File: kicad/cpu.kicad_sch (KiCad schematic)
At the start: 10 parts, among them U3 74HC138, U4 W65C02SxP, U6 74HC04, U7 74HC00

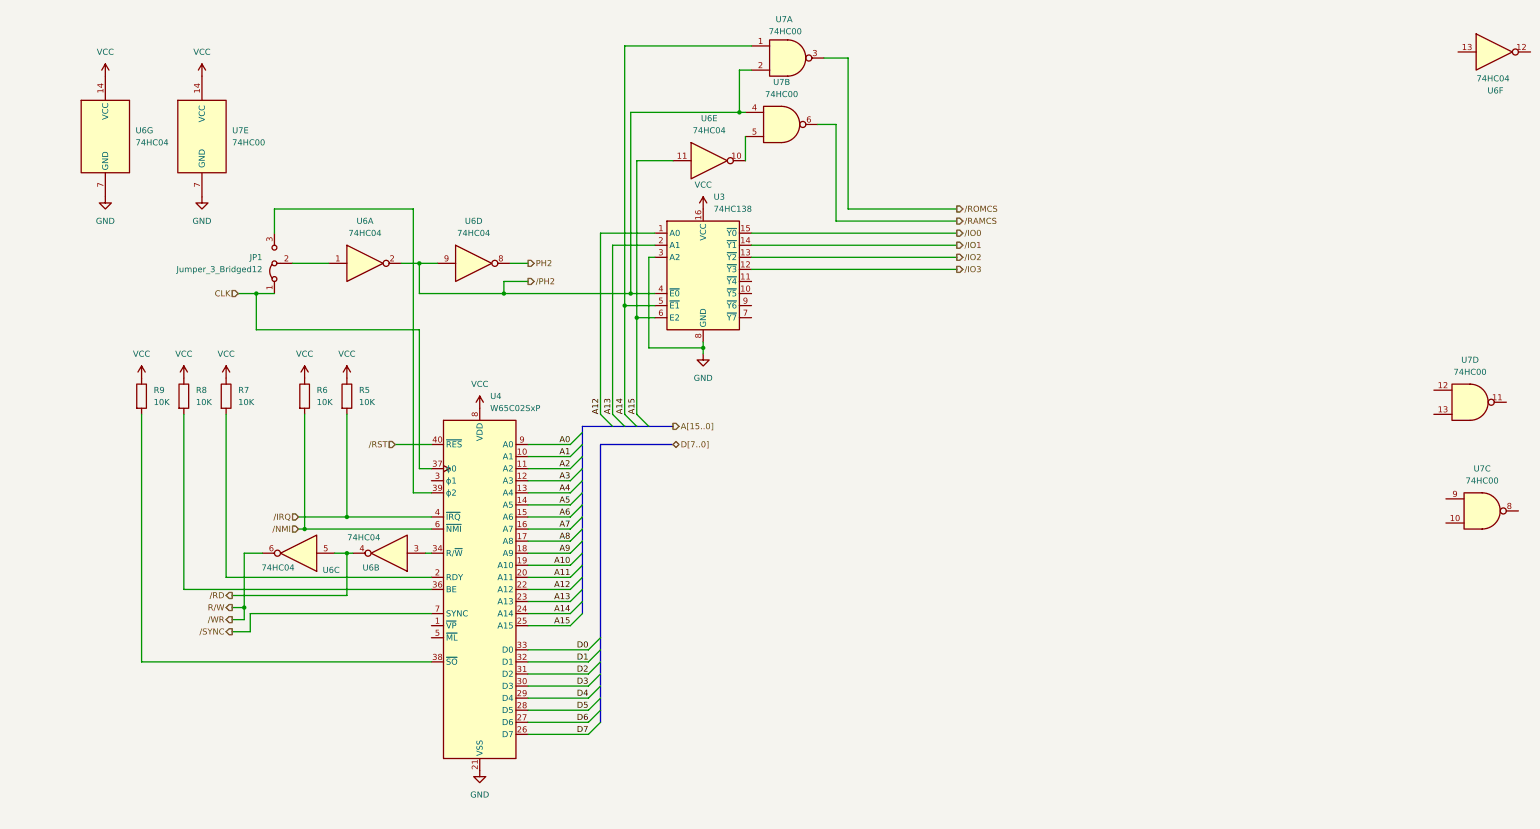
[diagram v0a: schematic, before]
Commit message: Add keyboard connector
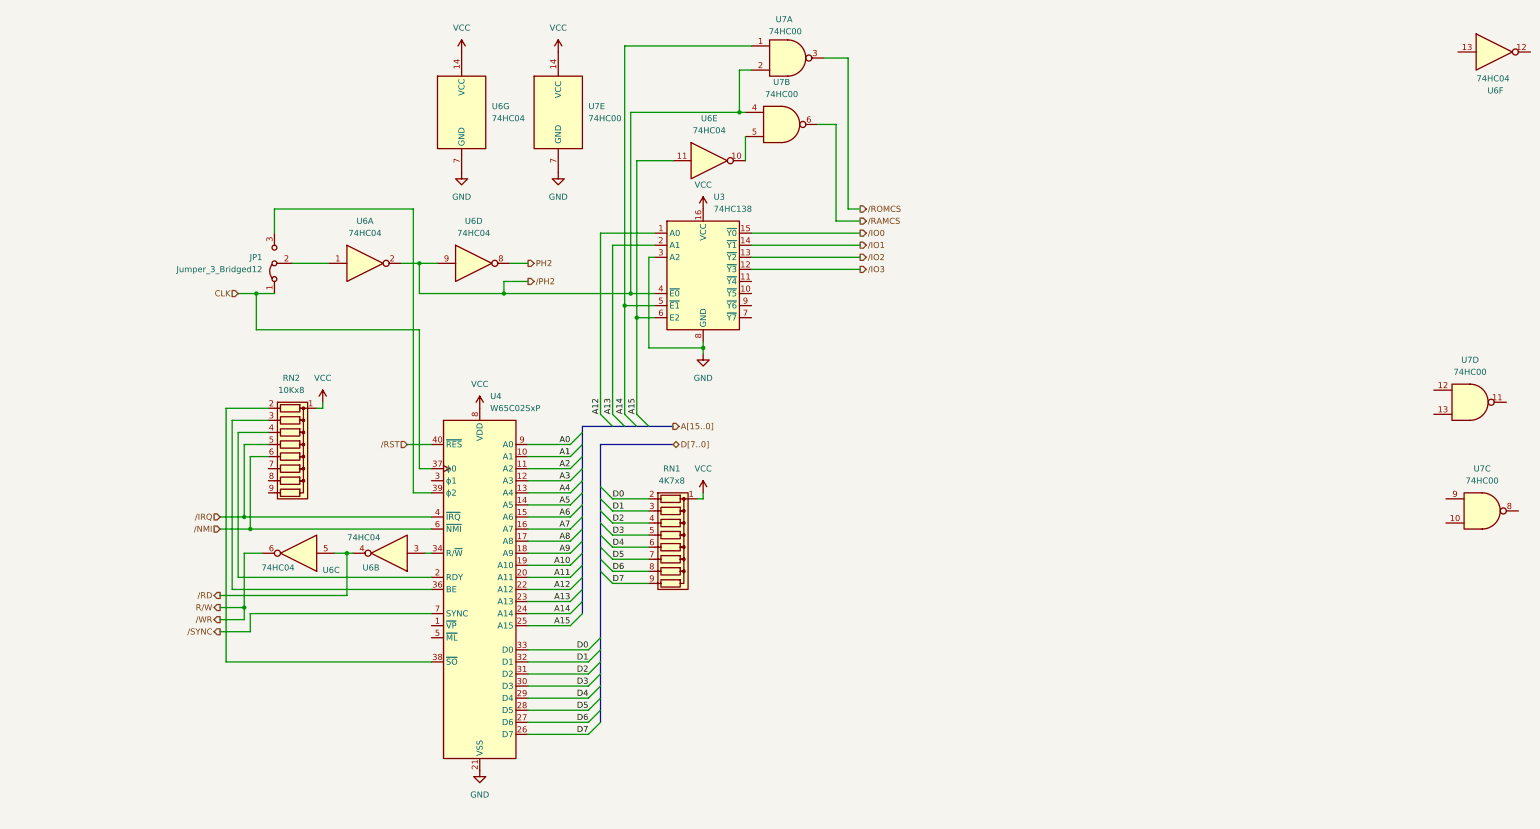
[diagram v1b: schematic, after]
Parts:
- removed R5, R6, R7, R8, R9: 10K, Resistor_THT:R_Axial_DIN0207_L6.3mm_D2.5mm_P7.62mm_Horizontal, symbol Device:R
- added RN1: 4K7x8, Resistor_THT:R_Array_SIP9, symbol Device:R_Network08
- added RN2: 10Kx8, Resistor_THT:R_Array_SIP9, symbol Device:R_Network08
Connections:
- net D0: now also RN1.2 (R1)
- net D1: now also RN1.3 (R2)
- net D2: now also RN1.4 (R3)
- net D3: now also RN1.5 (R4)
- net D4: now also RN1.6 (R5)
- net D5: now also RN1.7 (R6)
- net D6: now also RN1.8 (R7)
- net D7: now also RN1.9 (R8)
- net VCC: now also RN1.1 (common), RN2.1 (common)
- net /IRQ: now also RN2.5 (R4)
- net /NMI: now also RN2.6 (R5)
- net at U4.36 (BE): now also RN2.3 (R2)
- net at U4.38 (~{SO}): now also RN2.2 (R1)
- net at U4.2 (RDY): now also RN2.4 (R3)
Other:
- moved on the sheet: U6G, U7E

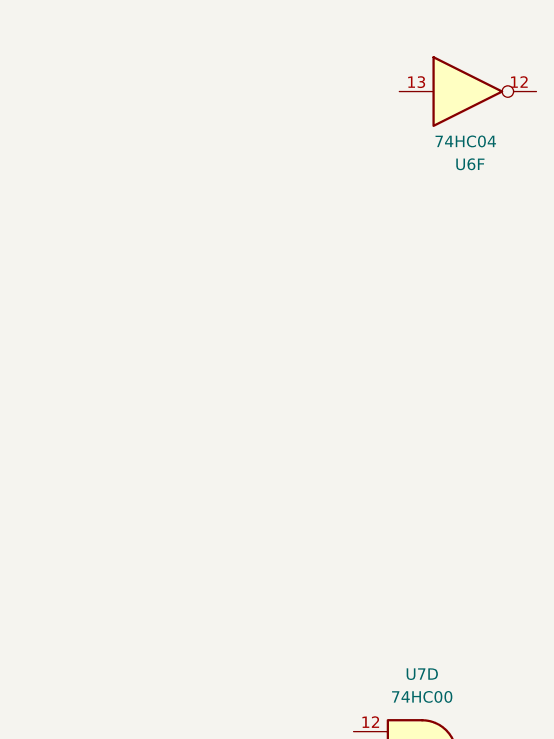
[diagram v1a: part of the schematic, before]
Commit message: Add user IO and USB
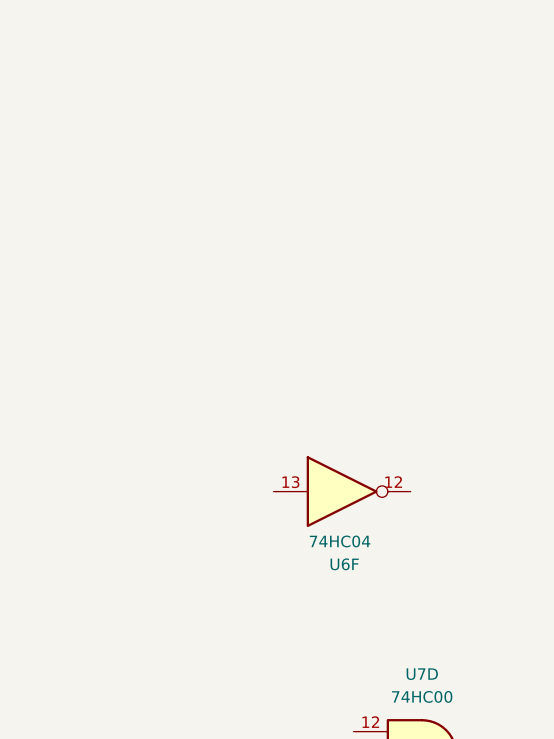
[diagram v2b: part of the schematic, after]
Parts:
- JP1: footprint (none) -> Jumper:SolderJumper-3_P1.3mm_Bridged12_Pad1.0x1.5mm
- U3: footprint (none) -> Package_DIP:DIP-16_W7.62mm
- U6, U7: footprint (none) -> Package_DIP:DIP-14_W7.62mm
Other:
- moved on the sheet: U6F
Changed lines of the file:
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@@
 			)
 		)
-		(property "Footprint" ""
+		(property "Footprint" "Package_DIP:DIP-14_W7.62mm"
 			(at 86.36 134.62 0)
 			(effects
@@
 	(symbol
 		(lib_id "74xx:74HC04")
-		(at 337.82 29.21 0)
+		(at 323.85 73.66 0)
 		(unit 6)
 		(exclude_from_sim no)
@@
 		(dnp no)
 		(property "Reference" "U6"
-			(at 338.074 37.338 0)
+			(at 324.104 81.788 0)
 			(effects
 				(font
@@
 		)
 		(property "Value" "74HC04"
-			(at 337.566 34.798 0)
-			(effects
-				(font
-					(size 1.27 1.27)
-				)
-			)
-		)
-		(property "Footprint" ""
-			(at 337.82 29.21 0)
+			(at 323.596 79.248 0)
+			(effects
+				(font
+					(size 1.27 1.27)
+				)
+			)
+		)
+		(property "Footprint" "Package_DIP:DIP-14_W7.62mm"
+			(at 323.85 73.66 0)
 			(effects
 				(font
@@
 		)
 		(property "Datasheet" "https://assets.nexperia.com/documents/data-sheet/74HC_HCT04.pdf"
-			(at 337.82 29.21 0)
+			(at 323.85 73.66 0)
 			(effects
 				(font
@@
 		)
 		(property "Description" "Hex Inverter"
-			(at 337.82 29.21 0)
+			(at 323.85 73.66 0)
 			(effects
 				(font
@@
 			)
 		)
-		(property "Footprint" ""
+		(property "Footprint" "Package_DIP:DIP-14_W7.62mm"
 			(at 105.41 134.62 0)
 			(effects
@@
 			)
 		)
-		(property "Footprint" ""
+		(property "Footprint" "Package_DIP:DIP-14_W7.62mm"
 			(at 335.28 125.73 0)
 			(effects
@@
 			)
 		)
-		(property "Footprint" ""
+		(property "Footprint" "Package_DIP:DIP-14_W7.62mm"
 			(at 123.19 73.66 0)
 			(effects
@@
 			)
 		)
-		(property "Footprint" ""
+		(property "Footprint" "Package_DIP:DIP-14_W7.62mm"
 			(at 332.74 102.87 0)
 			(effects
@@
 			)
 		)
-		(property "Footprint" ""
+		(property "Footprint" "Package_DIP:DIP-14_W7.62mm"
 			(at 100.33 73.66 0)
 			(effects
@@
 			)
 		)
-		(property "Footprint" ""
+		(property "Footprint" "Package_DIP:DIP-14_W7.62mm"
 			(at 187.96 44.45 0)
 			(effects
@@
 			)
 		)
-		(property "Footprint" ""
+		(property "Footprint" "Jumper:SolderJumper-3_P1.3mm_Bridged12_Pad1.0x1.5mm"
 			(at 81.28 73.66 0)
 			(effects
@@
 			)
 		)
-		(property "Footprint" ""
+		(property "Footprint" "Package_DIP:DIP-14_W7.62mm"
 			(at 120.65 41.91 0)
 			(effects
@@
 			)
 		)
-		(property "Footprint" ""
+		(property "Footprint" "Package_DIP:DIP-14_W7.62mm"
 			(at 189.23 30.48 0)
 			(effects
@@
 			)
 		)
-		(property "Footprint" ""
+		(property "Footprint" "Package_DIP:DIP-16_W7.62mm"
 			(at 171.45 77.47 0)
 			(effects
@@
 			)
 		)
-		(property "Footprint" ""
+		(property "Footprint" "Package_DIP:DIP-14_W7.62mm"
 			(at 172.72 52.07 0)
 			(effects
@@
 			)
 		)
-		(property "Footprint" ""
+		(property "Footprint" "Package_DIP:DIP-14_W7.62mm"
 			(at 140.97 41.91 0)
 			(effects

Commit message: Add expansion slot
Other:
- note added: "Can use plain 6502/65C02, W65C02 is here to handle its additional pins"
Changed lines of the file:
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@@
+		)
+	)
+	(text "Can use plain 6502/65C02,\nW65C02 is here to handle\nits additional pins"
+		(exclude_from_sim no)
+		(at 98.044 167.132 0)
+		(effects
+			(font
+				(size 1.27 1.27)
+			)
 		)
 	)

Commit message: Add caps and make initial placement
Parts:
- added C12, C13, C14, C15: 100n, Capacitor_THT:C_Disc_D5.0mm_W2.5mm_P2.50mm, symbol Device:C
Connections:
- net GND: now also U6.13, U7.10, U7.12, U7.13, U7.9, C12.2, C13.2, C14.2, C15.2
- net VCC: now also C12.1, C13.1, C14.1, C15.1
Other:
- moved on the sheet: U6F, U7C, U7D

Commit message: Bugfixes, start routing
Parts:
- removed unit 6 of U6
- added RN3, RN4: 4K7x8, Resistor_THT:R_Array_SIP9, symbol Device:R_Network08
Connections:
- net A0: now also RN3.2 (R1)
- net A1: now also RN3.3 (R2)
- net A10: now also RN4.4 (R3)
- net A11: now also RN4.5 (R4)
- net A12: now also RN4.6 (R5)
- net A13: now also RN4.7 (R6)
- net A14: now also RN4.8 (R7)
- net A15: now also U7.2
- net A2: now also RN3.4 (R3)
- net A3: now also RN3.5 (R4)
- net A4: now also RN3.6 (R5)
- net A5: now also RN3.7 (R6)
- net A6: now also RN3.8 (R7)
- net A7: now also RN3.9 (R8)
- net A8: now also RN4.2 (R1)
- net A9: now also RN4.3 (R2)
- net GND: no longer U7.10, U7.12, U7.13, U7.9
- net VCC: now also RN3.1 (common), RN4.1 (common)
- net /PH2: now also U7.13; no longer U7.2
- net /ROMCS: now also U7.11; no longer U7.3
- net at U7.8: now also U7.12
- new net: U7.10, U7.3, U7.9
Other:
- moved on the sheet: C12, C13, C14, C15, U6E, U7C, U7D

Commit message: Finished routing, HW prototype ready
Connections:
- net CLK: now also JP1.2 (C), U6.1
- net PH2: now also U7.13, U7.4
- net /PH2: no longer U7.13, U7.4
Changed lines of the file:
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@@
 	(paper "A4")
+	(junction
+		(at 86.36 73.66)
+		(diameter 0)
+		(color 0 0 0 0)
+	)
 	(junction
 		(at 111.76 73.66)
@@
 	)
 	(junction
+		(at 156.21 54.61)
+		(diameter 0)
+		(color 0 0 0 0)
+	)
+	(junction
 		(at 74.93 146.05)
 		(diameter 0)
@@
 	)
 	(junction
-		(at 156.21 80.01)
+		(at 81.28 80.01)
 		(diameter 0)
 		(color 0 0 0 0)
@@
 	)
 	(junction
+		(at 135.89 73.66)
+		(diameter 0)
+		(color 0 0 0 0)
+	)
+	(junction
 		(at 157.48 46.99)
 		(diameter 0)
@@
 		(color 0 0 0 0)
 	)
-	(junction
-		(at 156.21 54.61)
-		(diameter 0)
-		(color 0 0 0 0)
-	)
 	(bus_entry
 		(at 177.8 139.7)
@@
 	(wire
 		(pts
-			(xy 156.21 80.01) (xy 129.54 80.01)
+			(xy 129.54 80.01) (xy 161.29 80.01)
 		)
 		(stroke
@@
 		)
 	)
+	(wire
+		(pts
+			(xy 156.21 66.04) (xy 135.89 66.04)
+		)
+		(stroke
+			(width 0)
+			(type default)
+		)
+	)
 	(bus
 		(pts
@@
 	(wire
 		(pts
-			(xy 92.71 73.66) (xy 85.09 73.66)
+			(xy 92.71 73.66) (xy 86.36 73.66)
 		)
 		(stroke
@@
 	(wire
 		(pts
+			(xy 135.89 73.66) (xy 142.24 73.66)
+		)
+		(stroke
+			(width 0)
+			(type default)
+		)
+	)
+	(wire
+		(pts
 			(xy 181.61 74.93) (xy 246.38 74.93)
 		)
@@
 	(wire
 		(pts
+			(xy 156.21 54.61) (xy 156.21 66.04)
+		)
+		(stroke
+			(width 0)
+			(type default)
+		)
+	)
+	(wire
+		(pts
+			(xy 81.28 80.01) (xy 86.36 80.01)
+		)
+		(stroke
+			(width 0)
+			(type default)
+		)
+	)
+	(wire
+		(pts
 			(xy 74.93 111.76) (xy 74.93 127)
 		)
@@
 		)
 	)
-	(wire
-		(pts
-			(xy 156.21 80.01) (xy 156.21 54.61)
-		)
-		(stroke
-			(width 0)
-			(type default)
-		)
-	)
 	(bus
 		(pts
@@
 	(wire
 		(pts
+			(xy 86.36 73.66) (xy 85.09 73.66)
+		)
+		(stroke
+			(width 0)
+			(type default)
+		)
+	)
+	(wire
+		(pts
 			(xy 80.01 114.3) (xy 76.2 114.3)
 		)
@@
 	(wire
 		(pts
+			(xy 86.36 80.01) (xy 86.36 73.66)
+		)
+		(stroke
+			(width 0)
+			(type default)
+		)
+	)
+	(wire
+		(pts
 			(xy 198.12 44.45) (xy 195.58 44.45)
 		)
@@
 		)
 	)
-	(wire
-		(pts
-			(xy 156.21 80.01) (xy 161.29 80.01)
-		)
-		(stroke
-			(width 0)
-			(type default)
-		)
-	)
 	(bus
 		(pts
@@
 	(wire
 		(pts
+			(xy 135.89 66.04) (xy 135.89 73.66)
+		)
+		(stroke
+			(width 0)
+			(type default)
+		)
+	)
+	(wire
+		(pts
 			(xy 154.94 82.55) (xy 154.94 105.41)
 		)
@@
 	(wire
 		(pts
-			(xy 130.81 73.66) (xy 142.24 73.66)
-		)
-		(stroke
+			(xy 130.81 73.66) (xy 135.89 73.66)
+		)
+		(stroke

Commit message: hw: Start work on rev B
Changelog:
- fixed IO address decoder (removed /PH2 gating),
- added missing reset circuit capacitor,
- added hardware VGA scrolling,
- removed VGA column register, replaced with address bus,
- fixed values of R5 and R6.
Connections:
- net GND: now also U3.4 (~{E0})
- net /PH2: no longer names the net of U6.2, U6.9
- net /PH2: no longer U3.4 (~{E0})
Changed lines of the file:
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@@
 	)
 	(junction
-		(at 111.76 73.66)
-		(diameter 0)
-		(color 0 0 0 0)
-	)
-	(junction
-		(at 129.54 80.01)
-		(diameter 0)
-		(color 0 0 0 0)
-	)
-	(junction
 		(at 156.21 54.61)
 		(diameter 0)
@@
 	)
 	(junction
+		(at 160.02 80.01)
+		(diameter 0)
+		(color 0 0 0 0)
+	)
+	(junction
 		(at 77.47 80.01)
 		(diameter 0)
@@
 	(wire
 		(pts
-			(xy 160.02 91.44) (xy 160.02 72.39)
+			(xy 160.02 91.44) (xy 160.02 80.01)
 		)
 		(stroke
@@
 		)
 	)
-	(wire
-		(pts
-			(xy 129.54 80.01) (xy 161.29 80.01)
-		)
-		(stroke
-			(width 0)
-			(type default)
-		)
-	)
 	(bus
 		(pts
@@
 	(wire
 		(pts
-			(xy 142.24 76.2) (xy 129.54 76.2)
-		)
-		(stroke
-			(width 0)
-			(type default)
-		)
-	)
-	(wire
-		(pts
 			(xy 156.21 66.04) (xy 135.89 66.04)
 		)
@@
 	(wire
 		(pts
-			(xy 129.54 80.01) (xy 111.76 80.01)
-		)
-		(stroke
-			(width 0)
-			(type default)
-		)
-	)
-	(wire
-		(pts
 			(xy 134.62 160.02) (xy 147.32 160.02)
 		)
@@
 		)
 	)
+	(wire
+		(pts
+			(xy 160.02 80.01) (xy 160.02 72.39)
+		)
+		(stroke
+			(width 0)
+			(type default)
+		)
+	)
 	(bus
 		(pts
@@
 	(wire
 		(pts
-			(xy 107.95 73.66) (xy 111.76 73.66)
+			(xy 107.95 73.66) (xy 115.57 73.66)
 		)
 		(stroke
@@
 	(wire
 		(pts
-			(xy 111.76 73.66) (xy 115.57 73.66)
-		)
-		(stroke
-			(width 0)
-			(type default)
-		)
-	)
-	(wire
-		(pts
 			(xy 77.47 80.01) (xy 81.28 80.01)
 		)
@@
 	(wire
 		(pts
-			(xy 149.86 105.41) (xy 149.86 67.31)
+			(xy 160.02 80.01) (xy 161.29 80.01)
 		)
 		(stroke
@@
 	(wire
 		(pts
-			(xy 111.76 80.01) (xy 111.76 73.66)
+			(xy 149.86 105.41) (xy 149.86 67.31)
 		)
 		(stroke
@@
 		)
 	)
-	(wire
-		(pts
-			(xy 129.54 76.2) (xy 129.54 80.01)
-		)
-		(stroke
-			(width 0)
-			(type default)
-		)
-	)
 	(bus
 		(pts
@@
 		)
 	)
-	(hierarchical_label "{slash}PH2"
-		(shape output)
-		(at 142.24 76.2 0)
-		(fields_autoplaced yes)
-		(effects
-			(font
-				(size 1.27 1.27)
-			)
-			(justify left)
-		)
-	)
